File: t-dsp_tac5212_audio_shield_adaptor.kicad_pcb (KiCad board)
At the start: 2 copper layers, 26.5 x 61 mm, 23 parts, among them J21 jumper, U1 Teensy 4.1 - DEVKIT

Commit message: update usb-a connector
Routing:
- net 5V: track 41.9 -> 43.1 mm
- net USB_SHIELD2: track 29.3 -> 29.9 mm
- net 3.3V: track 93.5 -> 93.2 mm, vias 3 -> 4

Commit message: Update PCB layout
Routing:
- net GND: track 60.8 -> 74.6 mm, vias 4 -> 39

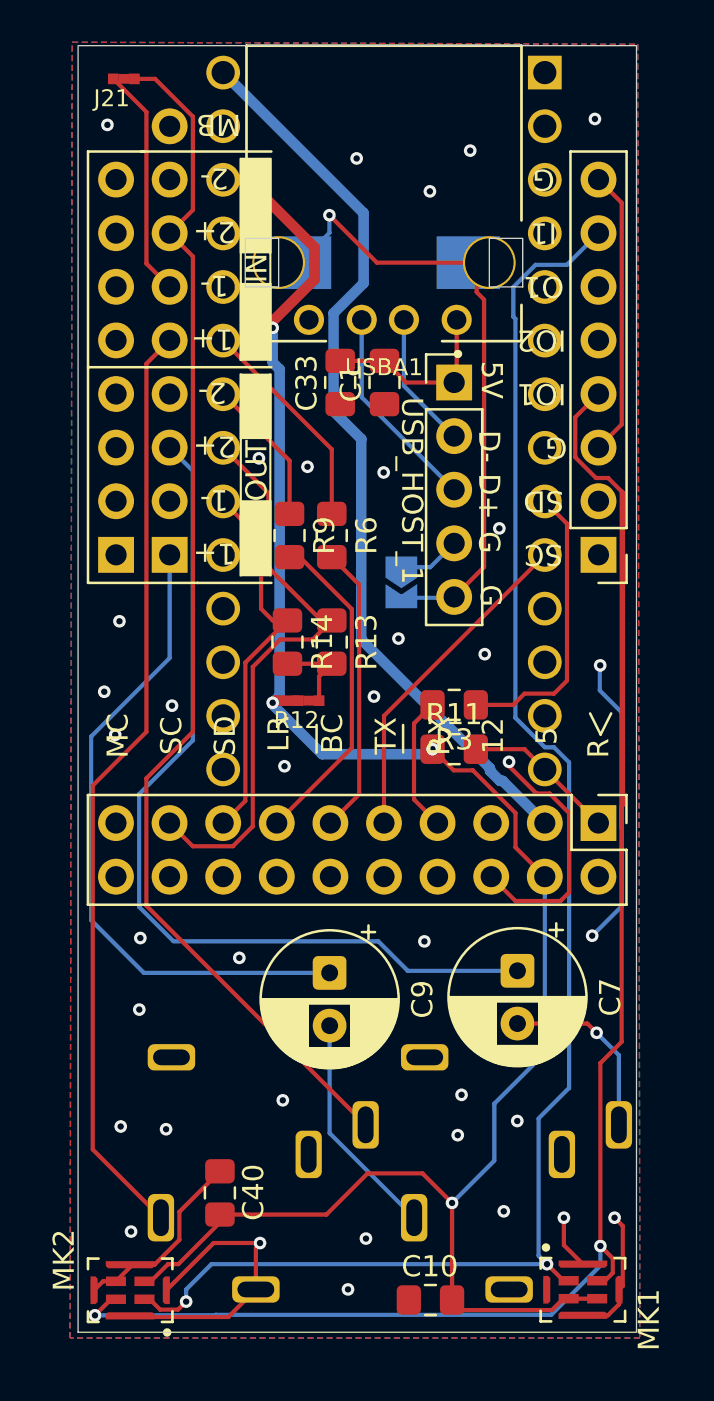
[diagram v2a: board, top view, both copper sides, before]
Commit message: Add new components, 3D models, and update PCB layout
Add footprints and symbols for BLM15AG601SN1D, MSM261DGT003,
PESD5V0F1BL_315, 35RAPC4BV4, and passive 0402 components.
Add corresponding 3D models. Update schematic, PCB layout,
and existing footprints.
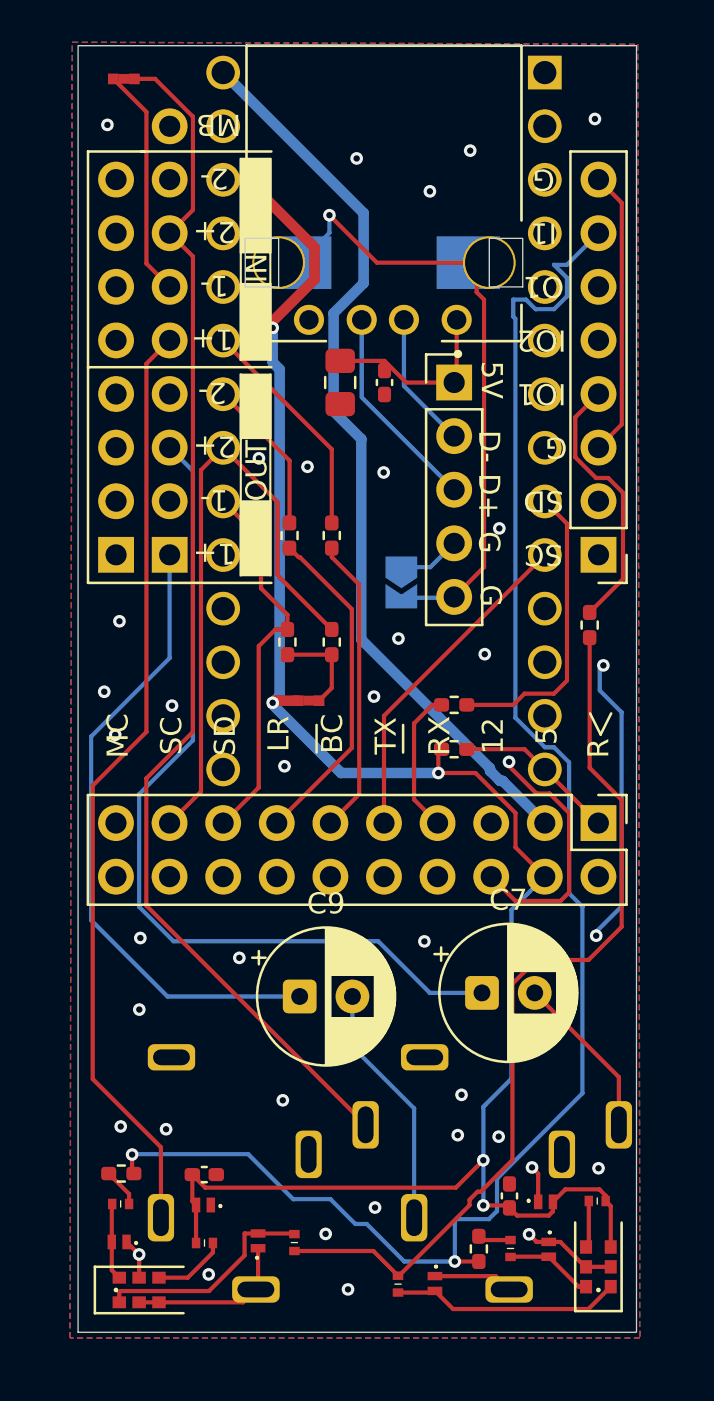
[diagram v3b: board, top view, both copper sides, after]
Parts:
- added D10: ~, project_fp:PESD5V0F1BL_315, F.Cu at (106.1, 197.7)
- added D11: ~, project_fp:PESD5V0F1BL_315, F.Cu at (114.4, 199.7)
- added D6: ~, project_fp:PESD5V0F1BL_315, F.Cu at (119.7, 195.8)
- added D7: ~, project_fp:PESD5V0F1BL_315, F.Cu at (103.5, 196.0)
- added D8: ~, project_fp:PESD5V0F1BL_315, F.Cu at (99.5, 197.7)
- added D9: ~, project_fp:PESD5V0F1BL_315, F.Cu at (119.8, 198.1)
- added FB1: 600Ω@100MHz, project_fp:BLM15AG601SN1D, F.Cu at (118.0, 198.0)
- added FB2: 600Ω@100MHz, project_fp:BLM15AG601SN1D, F.Cu at (99.5, 195.9)
- added FB3: 600Ω@100MHz, project_fp:BLM15AG601SN1D, F.Cu at (107.8, 197.7)
- added FB4: 600Ω@100MHz, project_fp:BLM15AG601SN1D, F.Cu at (112.7, 199.7)
- added FB5: 600Ω@100MHz, project_fp:BLM15AG601SN1D, F.Cu at (122.1, 195.8)
- added FB6: 600Ω@100MHz, project_fp:BLM15AG601SN1D, F.Cu at (103.5, 197.8)
- added R55: 49.9 ohm, project_fp:R_0402_1005Metric_Pad0.72x0.64mm_HandSolder, F.Cu at (121.8, 168.5)
- added R56: 49.9 ohm, project_fp:R_0402_1005Metric_Pad0.72x0.64mm_HandSolder, F.Cu at (99.6, 194.5)
- added R57: 49.9 ohm, project_fp:R_0402_1005Metric_Pad0.72x0.64mm_HandSolder, F.Cu at (116.5, 198.0)
- C1, C10, C40: footprint project_fp:C_0805_2012Metric_Pad1.15x1.40mm_HandSolder -> project_fp:C_0402_1005Metric_Pad0.74x0.62mm_HandSolder
- MK1, MK2: value SPK0641HT4H-1 -> MSM261DGT003; footprint project_fp:SPK0641HT4H-1 -> project_fp:MSM261DGT003
- R11, R13, R14, R3, R6, R9: footprint project_fp:R_0805_2012Metric_Pad1.15x1.40mm_HandSolder -> project_fp:R_0402_1005Metric_Pad0.72x0.64mm_HandSolder
- moved C40 13.7 mm to (118.0, 195.5)
- moved C10 12.3 mm to (103.5, 194.5), turned to 0 degrees
- moved C7 1.98 mm to (116.7, 185.9), turned to 0 degrees
- moved C9 1.81 mm to (108.0, 186.1), turned to 0 degrees
- moved MK1 0.74 mm to (122.2, 200.0), turned to 180 degrees
- moved MK2 0.68 mm to (99.3, 200.0)
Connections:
- MK1 pad 1: GPIGPI1 -> Net-(MK1-VDD)
- MK1 pad 2: GPIO1 -> GND
- MK1 pad 3: 3.3V -> Net-(D9-A)
- MK1 pad 4: 3.3V -> Net-(D11-A)
- MK1 pad 6: GND -> 3.3V
- MK2 pad 1: GPIGPI1 -> Net-(MK2-VDD)
- MK2 pad 2: GPIO1 -> GND
- MK2 pad 3: GND -> Net-(D8-A)
- MK2 pad 4: 3.3V -> Net-(D10-A)
- board_outline1 pad 40: GPIO1 -> Net-(board_outline1-GPIO1)
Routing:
- net GPIO1: track 88.0 -> 42.2 mm, vias 2 -> 0
- net Net-(board_outline1-GPIO1): track 0.00 -> 12.7 mm
- net GND: track 74.6 -> 62.2 mm, vias 39 -> 40
- net Net-(D11-A): track 0.00 -> 10.9 mm
- net Net-(D10-A): track 0.00 -> 10.6 mm
- net Net-(D9-A): track 0.00 -> 4.17 mm
- net Net-(D8-A): track 0.00 -> 3.65 mm
- net Net-(MK2-VDD): track 0.00 -> 3.50 mm
- net Net-(MK1-VDD): track 0.00 -> 2.23 mm
- net GPIGPI1: track 75.4 -> 77.5 mm
- net SCL0: track 27.6 -> 29.6 mm
- net Net-(FB2-Pad1): track 0.00 -> 1.84 mm
- net Net-(FB1-Pad1): track 0.00 -> 1.57 mm
- net 3.3V: track 93.4 -> 91.9 mm, vias 4 -> 5
- net /AUDIO_OUT2P: track 42.5 -> 41.2 mm
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
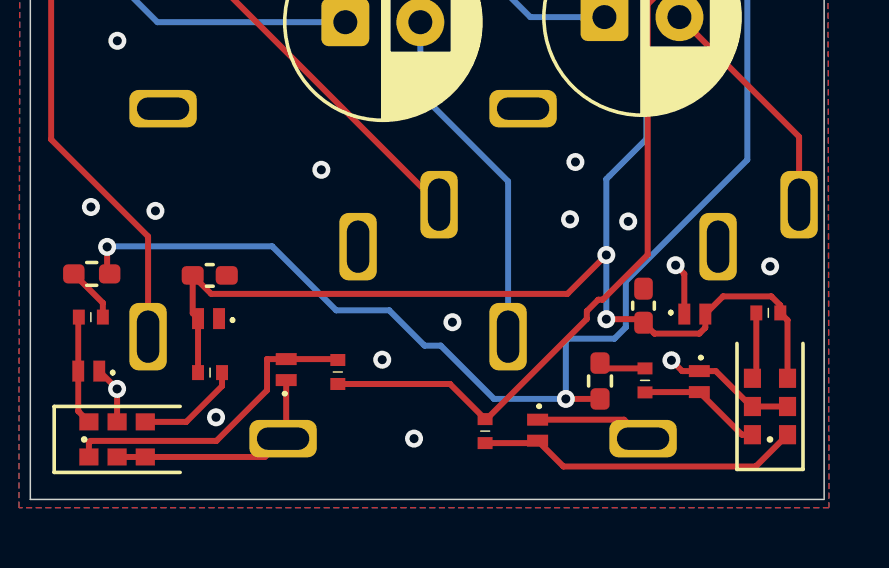
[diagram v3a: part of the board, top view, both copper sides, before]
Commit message: Fix ESD diode values and R13 value format for BOM correctness
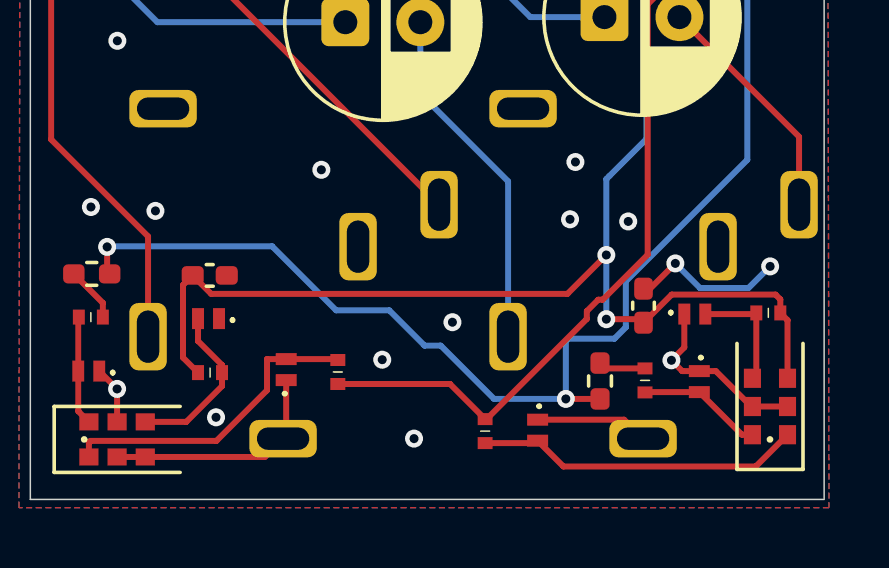
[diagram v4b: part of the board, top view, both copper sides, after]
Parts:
- D10, D11, D6, D7, D8, D9: value ~ -> ESD DIODE
- R13, R14: value 2.21k ohm -> 2.21k
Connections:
- D6 pad 2: 3.3V -> Net-(D6-A)
- D7 pad 2: 3.3V -> Net-(D7-A)
- FB5 pad 2: Net-(MK1-VDD) -> Net-(D6-A)
- FB6 pad 2: Net-(MK2-VDD) -> Net-(D7-A)
- MK1 pad 1: Net-(MK1-VDD) -> Net-(D6-A)
- MK2 pad 1: Net-(MK2-VDD) -> Net-(D7-A)
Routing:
- net Net-(D7-A): track 0.00 -> 5.63 mm
- net GND: track 62.2 -> 67.4 mm
- net Net-(D6-A): track 0.00 -> 3.95 mm
- net Net-(MK2-VDD): track 3.50 -> 0.00 mm
- net Net-(MK1-VDD): track 2.23 -> 0.00 mm
